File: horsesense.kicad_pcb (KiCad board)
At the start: 4 copper layers, 30 x 60 mm, 72 parts, among them IC1 BGA824N6E6329XTSA1, J1 GT-USB-7025, J2 S2B-PH-SM4-TB, J3 73412-0110, J4 Conn_01x04, Q1 RE1C002UNTCL, SW1 EVQP7A01P, SW2 EVQP7A01P, U1 MAX86141ENP+T, U10 MAX-M8Q, U2 TXB0304RUTR, U3 BQ25601, U4 XC6210B332MR, U5 XC6210B182MR, U6 MAX4740ETE_, U8 MX25L3233FM2I-08G, U9 ESP32-S3-WROOM-1-N16R8

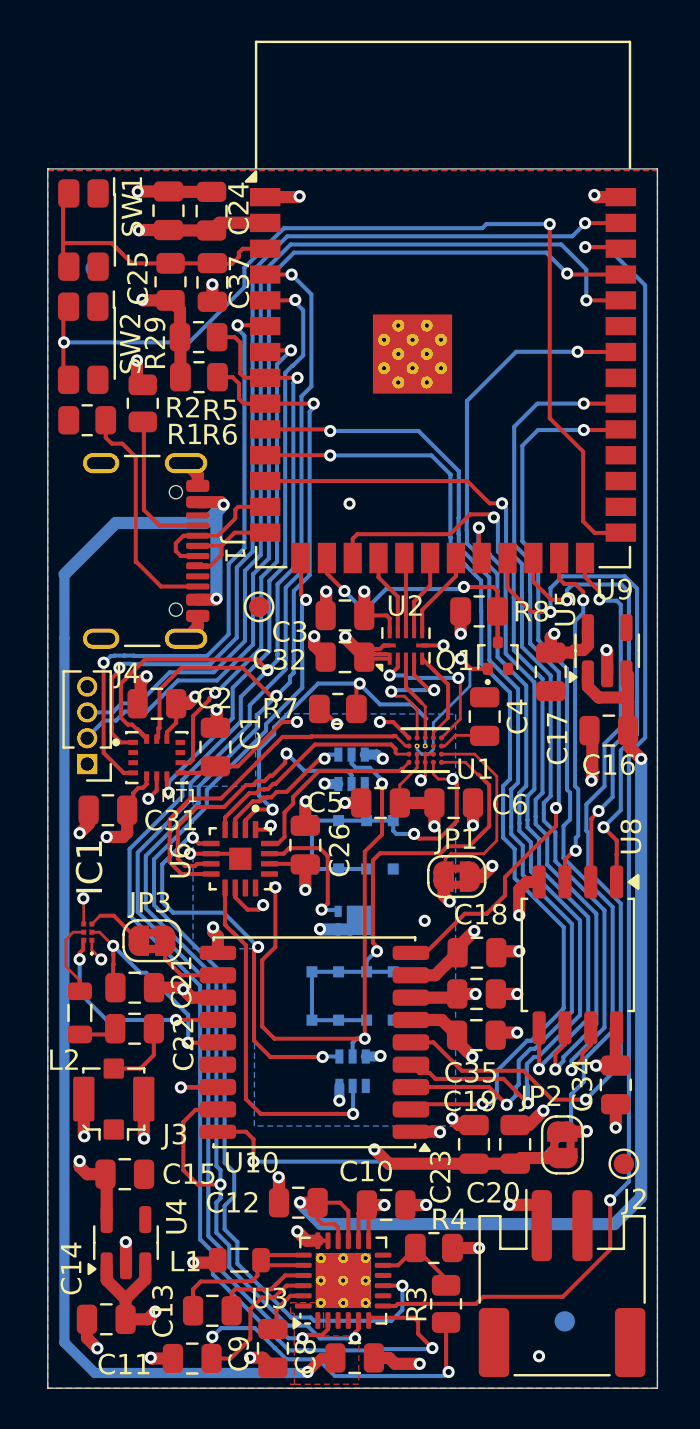
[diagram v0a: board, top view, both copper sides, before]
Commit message: PCP correction CAO fitback
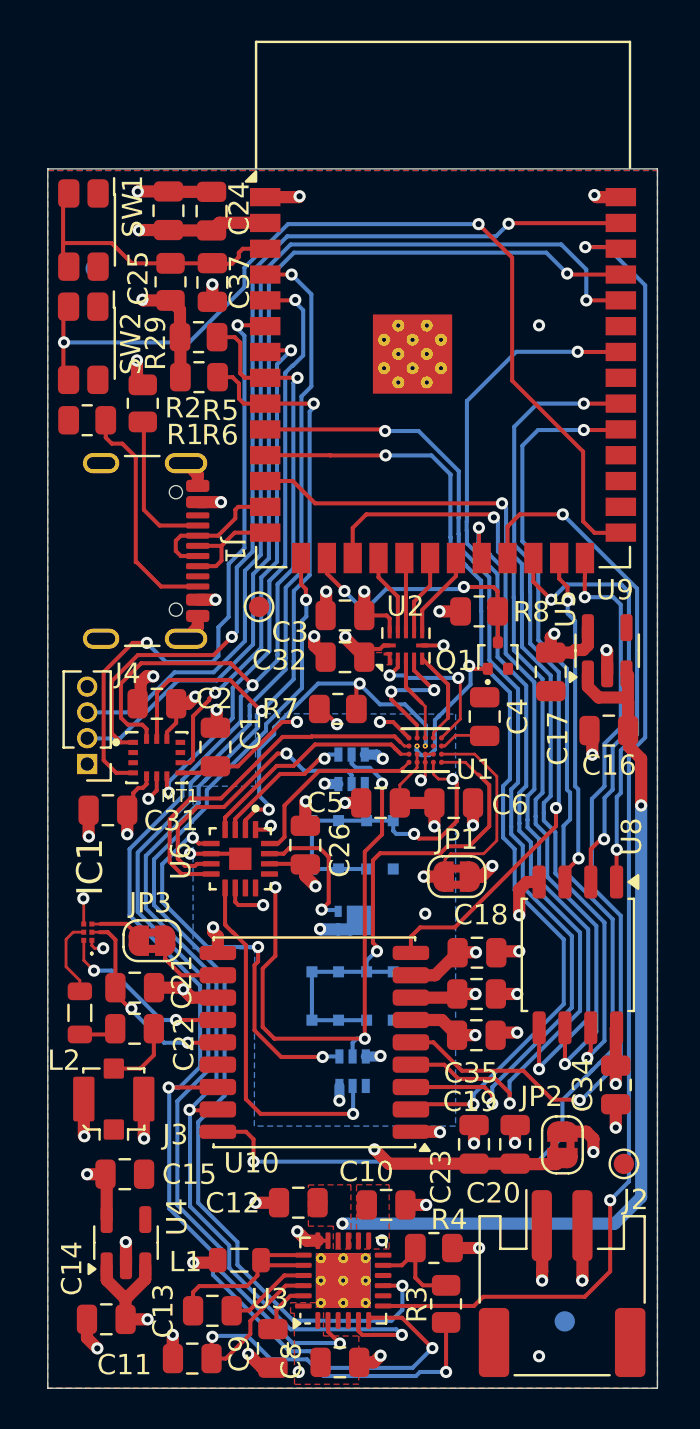
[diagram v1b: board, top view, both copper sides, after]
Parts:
- moved C8 0.76 mm to (154.1, 142.7)
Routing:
- net Vsys: track 62.7 -> 53.2 mm
- net VBUS: track 68.4 -> 63.7 mm
- net +BATT: track 6.88 -> 3.57 mm
- net PSEL_BAT: track 63.3 -> 66.0 mm
- net +1.8V: track 15.0 -> 12.9 mm
- net Net-(U9-IO0): track 48.1 -> 46.0 mm
- net FLASH_SID3: track 45.5 -> 43.7 mm
- net +3.3V: track 51.0 -> 49.2 mm
- net SCL: track 78.8 -> 77.6 mm
- net Net-(IC1-PON): track 9.99 -> 8.88 mm
- net Net-(IC1-VCC): track 11.4 -> 10.3 mm
- net ICM_INT: track 30.3 -> 31.4 mm
- net GPIO1: track 26.6 -> 25.6 mm
- net MAX_INT_1_8: track 8.12 -> 7.21 mm
- net FLASH_CS: track 25.4 -> 24.5 mm
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- added copper zone on F.Cu, net +1.8V
- added copper zone on F.Cu, net +BATT
- added copper zone on F.Cu, net Vsys

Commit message: Correction from feedback jlcpcb
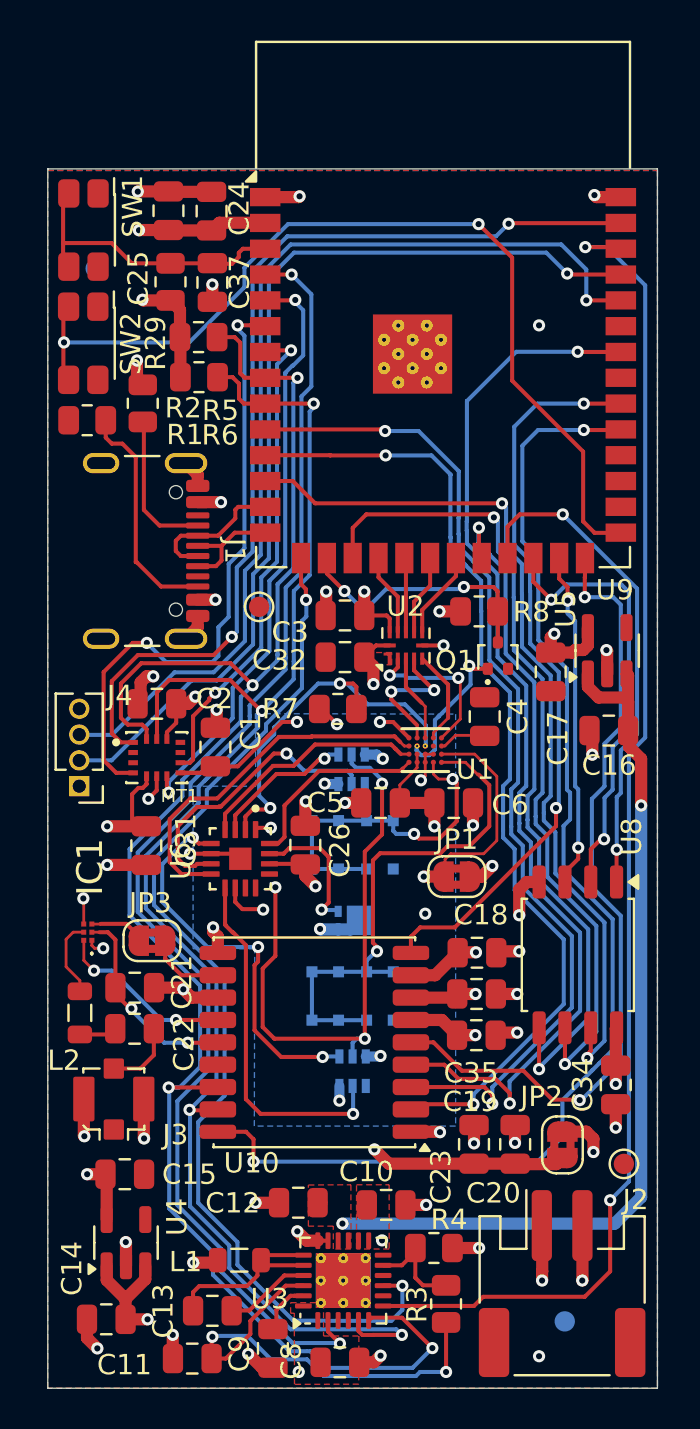
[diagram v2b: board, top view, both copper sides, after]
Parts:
- moved C31 2.57 mm to (144.5, 117.3), turned to -90 degrees
- moved J4 1.16 mm to (141.2, 114.4)
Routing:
- net GND: track 66.9 -> 65.6 mm, vias 47 -> 46
- net GPIO1: track 25.6 -> 26.8 mm
- net +3.3V: track 49.2 -> 50.3 mm
- net Net-(J4-Pin_3): track 47.9 -> 48.8 mm
- net Net-(J4-Pin_2): track 46.8 -> 47.6 mm
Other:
- rule pad_to_mask_clearance: 0 -> 0.03
